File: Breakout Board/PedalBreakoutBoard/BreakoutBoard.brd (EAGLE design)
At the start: 100 x 80 mm, 45 parts, among them U1 ES_DAISY_SEED_REV4

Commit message: DP-16 - Board layout REV-A
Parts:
- removed 1P8T: (no value), SparkFun-Connectors:1X09
- removed GPIOS: (no value), SparkFun-Connectors:1X07
- removed IN_L, IN_R, LED1, LED2, LED3, LED4, OUT_L, OUT_R, SPST1, SPST2, SPST3, SPST4: (no value), SparkFun-Connectors:1X02
- removed POT1, POT2, POT3, POT4, SPDT1, SPDT2: (no value), SparkFun-Connectors:1X03
- added 1P8T_GPIO: (no value), SparkFun-Connectors:1X08
- added 1P8T_PWR: (no value), SparkFun-Connectors:1X01
- added AUDIO, EX_GND, EX_PWR: (no value), SparkFun-Connectors:2X4
- added EX_GPIOS: (no value), SparkFun-Connectors:1X07
- added LED_GND, LED_GPIO, POT_GND, POT_GPIO, POT_PWR, SPDT_GPIO, SPST_GPIO, SPST_PWR: (no value), SparkFun-Connectors:1X04
- added SPDT_PWR: (no value), SparkFun-Connectors:1X02
- moved S1 31.9 mm to (27.9, 47.0)
- moved S2 30.7 mm to (27.9, 44.5)
- moved S3 29.5 mm to (27.9, 41.9)
- moved S4 28.4 mm to (27.9, 39.4)
- moved D11 27.5 mm to (27.9, 36.8)
- moved D12 25.4 mm to (27.9, 34.3)
- moved D21 24.4 mm to (27.9, 31.8)
- moved D22 22.5 mm to (27.9, 29.2)
- moved D1 20.7 mm to (76.2, 62.2)
- moved L4 20.7 mm to (69.8, 19.1)
- moved L3 19.8 mm to (69.8, 21.6)
- moved C3 18.9 mm to (67.3, 63.5), turned to 90 degrees
- moved L2 18.9 mm to (69.8, 24.1)
- moved L1 18.1 mm to (69.8, 26.7)
- moved 8T2 17.3 mm to (73.7, 54.6)
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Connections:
- removed net GPIO10: GPIOS.6, U1.10
- removed net GPIO11: GPIOS.5, U1.11
- removed net GPIO12: GPIOS.4, U1.12
- removed net GPIO13: GPIOS.3, U1.13
- removed net GPIO14: GPIOS.2, U1.14
- removed net GPIO15: GPIOS.1, U1.15
- removed net GPIO9: GPIOS.7, U1.9
- removed net N$6: L2.P$2, LED2.1
- removed net N$7: L3.P$2, LED3.1
- removed net N$8: L4.P$2, LED4.1
- new net GPIO1: EX_GPIOS.7, U1.1
- new net GPIO2: EX_GPIOS.6, U1.2
- new net GPIO3: EX_GPIOS.5, U1.3
- new net GPIO4: EX_GPIOS.4, U1.4
- new net GPIO5: EX_GPIOS.3, U1.5
- new net GPIO6: EX_GPIOS.2, U1.6
- new net GPIO7: EX_GPIOS.1, U1.7
- new net N$1: L1.P$2, LED_GPIO.1
- new net N$3: L2.P$2, LED_GPIO.2
- new net N$4: L3.P$2, LED_GPIO.3
- net +3V3_A: now also 1P8T_PWR.1, EX_PWR.1, EX_PWR.2, EX_PWR.3, EX_PWR.4, EX_PWR.5, EX_PWR.6, EX_PWR.7, EX_PWR.8, POT_PWR.1, POT_PWR.2, POT_PWR.3, POT_PWR.4, SPDT_PWR.1, SPDT_PWR.2, SPST_PWR.1, SPST_PWR.2, SPST_PWR.3, SPST_PWR.4; no longer 1P8T.9, POT1.1, POT2.1, POT3.1, POT4.1, SPDT1.2, SPDT2.2, SPST1.1, SPST2.1, SPST3.1, SPST4.1
- net 1P8T_1: now also 1P8T_GPIO.1; no longer 1P8T.1
- net 1P8T_2: now also 1P8T_GPIO.2; no longer 1P8T.2
- net 1P8T_3: now also 1P8T_GPIO.3; no longer 1P8T.3
- net 1P8T_4: now also 1P8T_GPIO.4; no longer 1P8T.4
- net 1P8T_5: now also 1P8T_GPIO.5; no longer 1P8T.5
- net 1P8T_6: now also 1P8T_GPIO.6; no longer 1P8T.6
- net 1P8T_7: now also 1P8T_GPIO.7; no longer 1P8T.7
- net 1P8T_8: now also 1P8T_GPIO.8; no longer 1P8T.8
- net GND: now also AUDIO.1, AUDIO.3, AUDIO.5, AUDIO.7, EX_GND.1, EX_GND.2, EX_GND.3, EX_GND.4, EX_GND.5, EX_GND.6, EX_GND.7, EX_GND.8, LED_GND.1, LED_GND.2, LED_GND.3, LED_GND.4, POT_GND.1, POT_GND.2, POT_GND.3, POT_GND.4; no longer IN_L.1, IN_R.1, LED1.2, LED2.2, LED3.2, LED4.2, OUT_L.1, OUT_R.1, POT1.3, POT2.3, POT3.3, POT4.3
- net IN_L: now also AUDIO.2; no longer IN_L.2
- net IN_R: now also AUDIO.4; no longer IN_R.2
- net N$5: now also L4.P$2, LED_GPIO.4; no longer L1.P$2, LED1.1
- net OUT_L: now also AUDIO.6; no longer OUT_L.2
- net OUT_R: now also AUDIO.8; no longer OUT_R.2
- net POT1: now also POT_GPIO.1; no longer POT1.2
- net POT2: now also POT_GPIO.2; no longer POT2.2
- net POT3: now also POT_GPIO.3; no longer POT3.2
- net POT4: now also POT_GPIO.4; no longer POT4.2
- net SPDT1_1: now also SPDT_GPIO.4, U1.12; no longer SPDT1.3, U1.5
- net SPDT1_2: now also SPDT_GPIO.3, U1.13; no longer SPDT1.1, U1.6
- net SPDT2_1: now also SPDT_GPIO.2, U1.14; no longer SPDT2.3, U1.7
- net SPDT2_2: now also SPDT_GPIO.1, U1.15; no longer SPDT2.1, U1.8
- net SPST1: now also SPST_GPIO.4, U1.8; no longer SPST1.2, U1.1
- net SPST2: now also SPST_GPIO.3, U1.9; no longer SPST2.2, U1.2
- net SPST3: now also SPST_GPIO.2, U1.10; no longer SPST3.2, U1.3
- net SPST4: now also SPST_GPIO.1, U1.11; no longer SPST4.2, U1.4

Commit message: DP-16 - Board layout REV-B
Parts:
- removed 1P8T_GPIO: (no value), SparkFun-Connectors:1X08
- removed 1P8T_PWR: (no value), SparkFun-Connectors:1X01
- removed 8T1, 8T2, 8T3, 8T4: 10k, SparkFun-Resistors:AXIAL-0.3
- added HEX_GPIO: (no value), SparkFun-Connectors:1X04
- added HEX_PWR: (no value), SparkFun-Connectors:1X01
- EX_GND, EX_PWR: device SparkFun-Connectors:2X4 -> SparkFun-Connectors:1X04
- EX_GPIOS: device SparkFun-Connectors:1X07 -> SparkFun-Connectors:1X04
- moved 8T7 7.62 mm to (73.7, 49.5)
- moved 8T8 7.62 mm to (73.7, 47.0)
- moved 8T5 7.62 mm to (73.7, 54.6)
- moved 8T6 7.62 mm to (73.7, 52.1)
- moved EX_GPIOS 7.62 mm to (35.6, 57.1)
- moved EX_PWR 6.48 mm to (27.9, 57.1), turned to 90 degrees
- moved EX_GND 5.24 mm to (31.8, 57.1), turned to 90 degrees
- moved S3 5.08 mm to (27.9, 47.0)
- moved S4 5.08 mm to (27.9, 44.5)
- moved SPST_GPIO 5.08 mm to (35.6, 44.5)
- moved SPST_PWR 5.08 mm to (20.3, 44.5)
- moved S1 5.08 mm to (27.9, 52.1)
- moved S2 5.08 mm to (27.9, 49.5)
- moved AUDIO 2.54 mm to (34.3, 22.9)
- moved D11 2.54 mm to (27.9, 39.4)
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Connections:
- removed net 1P8T_1: 1P8T_GPIO.1, 8T1.P$2, U1.37
- removed net 1P8T_2: 1P8T_GPIO.2, 8T2.P$2, U1.36
- removed net 1P8T_3: 1P8T_GPIO.3, 8T3.P$2, U1.35
- removed net 1P8T_4: 1P8T_GPIO.4, 8T4.P$2, U1.34
- removed net 1P8T_5: 1P8T_GPIO.5, 8T5.P$2, U1.33
- removed net 1P8T_6: 1P8T_GPIO.6, 8T6.P$2, U1.32
- removed net 1P8T_7: 1P8T_GPIO.7, 8T7.P$2, U1.31
- removed net 1P8T_8: 1P8T_GPIO.8, 8T8.P$2, U1.30
- removed net GPIO5: EX_GPIOS.3, U1.5
- removed net GPIO6: EX_GPIOS.2, U1.6
- removed net GPIO7: EX_GPIOS.1, U1.7
- new net HEX_1: 8T5.P$2, HEX_GPIO.1, U1.36
- new net HEX_2: 8T6.P$2, HEX_GPIO.2, U1.35
- new net HEX_3: 8T7.P$2, HEX_GPIO.3, U1.34
- new net HEX_4: 8T8.P$2, HEX_GPIO.4, U1.33
- net +3V3_A: now also HEX_PWR.1; no longer 1P8T_PWR.1, EX_PWR.5, EX_PWR.6, EX_PWR.7, EX_PWR.8
- net GND: no longer 8T1.P$1, 8T2.P$1, 8T3.P$1, 8T4.P$1, EX_GND.5, EX_GND.6, EX_GND.7, EX_GND.8
- net GPIO1: now also EX_GPIOS.4; no longer EX_GPIOS.7
- net GPIO2: now also EX_GPIOS.3; no longer EX_GPIOS.6
- net GPIO3: now also EX_GPIOS.2; no longer EX_GPIOS.5
- net GPIO4: now also EX_GPIOS.1; no longer EX_GPIOS.4
- net POT1: now also U1.30; no longer U1.29
- net POT2: now also U1.29; no longer U1.28
- net POT3: now also U1.28; no longer U1.27
- net POT4: now also U1.27; no longer U1.26
- net SPDT1_1: now also U1.11; no longer U1.12
- net SPDT1_2: now also U1.12; no longer U1.13
- net SPDT2_1: now also U1.13; no longer U1.14
- net SPDT2_2: now also U1.14; no longer U1.15
- net SPST1: now also U1.6; no longer U1.8
- net SPST2: now also U1.7; no longer U1.9
- net SPST3: now also U1.8; no longer U1.10
- net SPST4: now also U1.9; no longer U1.11
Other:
- board size 100 x 80 mm -> 68.2 x 63.5 mm

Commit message: DP-16 - Initial routing
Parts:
- moved L1 22.2 mm to (50.8, 15.2)
- moved L2 22.2 mm to (50.8, 12.7)
- moved L3 22.2 mm to (50.8, 10.2)
- moved L4 22.2 mm to (50.8, 7.62)
- moved LED_GPIO 22.2 mm to (58.4, 15.2)
- moved D1 21.1 mm to (58.4, 50.8)
- moved C3 20.1 mm to (50.8, 52.1)
- moved D12 20.1 mm to (11.4, 25.4)
- moved D21 20.1 mm to (11.4, 22.9)
- moved D22 20.1 mm to (11.4, 20.3)
- moved EX_GPIOS 20.1 mm to (19.1, 45.7)
- moved EX_PWR 20.1 mm to (11.4, 45.7)
- moved HEX_GPIO 20.1 mm to (49.5, 43.2)
- moved POT_GPIO 20.1 mm to (49.5, 27.9)
- moved PWR 20.1 mm to (57.1, 54.6)
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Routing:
- net GND: track 0.00 -> 176.9 mm, vias 0 -> 1
- net +3V3_A: track 0.00 -> 146.0 mm, vias 0 -> 1
- net +9V_IN: track 0.00 -> 14.8 mm
- net HEX_4: track 0.00 -> 11.6 mm
- net HEX_2: track 0.00 -> 11.6 mm
- net SPST4: track 0.00 -> 11.6 mm
- net SPST2: track 0.00 -> 11.6 mm
- net SPDT2_1: track 0.00 -> 11.6 mm
- net SPDT1_1: track 0.00 -> 11.6 mm
- net HEX_3: track 0.00 -> 11.3 mm
- net HEX_1: track 0.00 -> 11.3 mm
- net SPST3: track 0.00 -> 11.3 mm
- net SPST1: track 0.00 -> 11.3 mm
- net SPDT2_2: track 0.00 -> 11.3 mm
- net SPDT1_2: track 0.00 -> 11.3 mm
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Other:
- board size 68.2 x 63.5 mm -> 64.4 x 58.4 mm

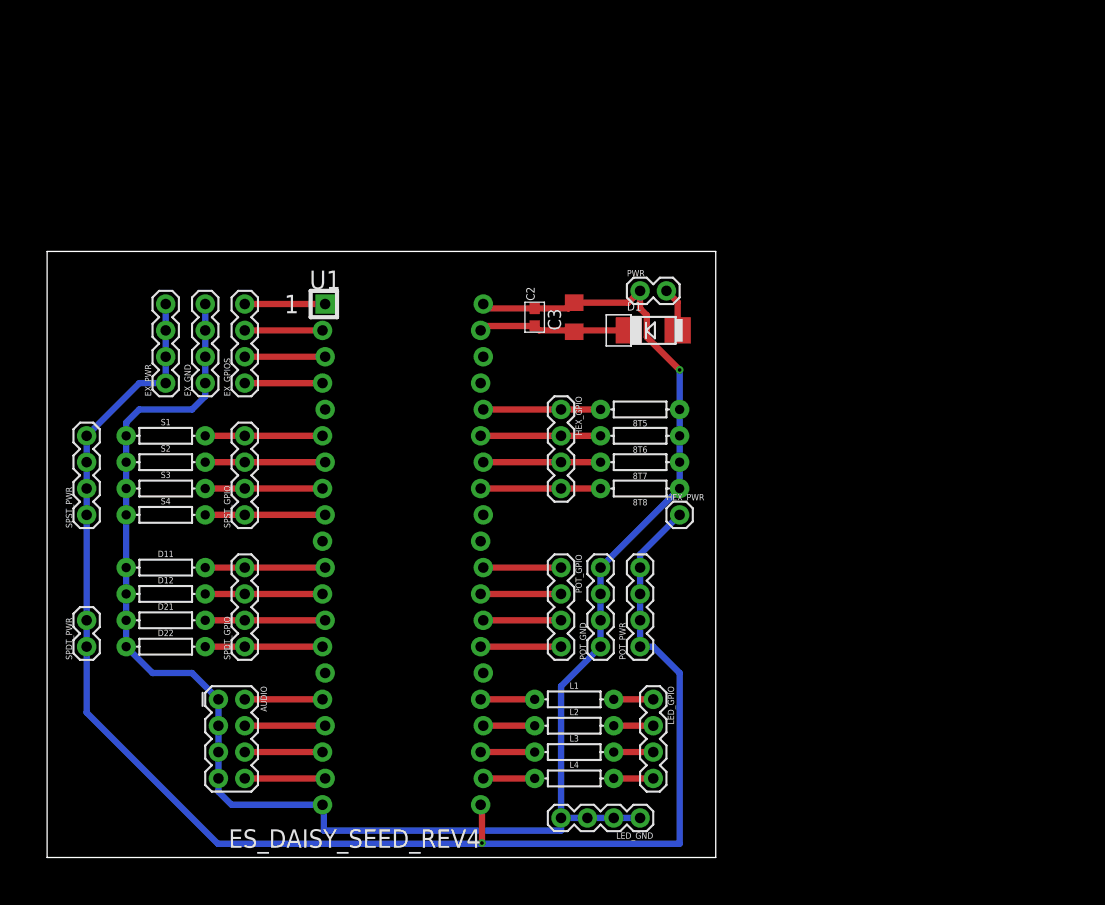
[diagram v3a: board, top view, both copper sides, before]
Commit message: DP-16 - Update board layout
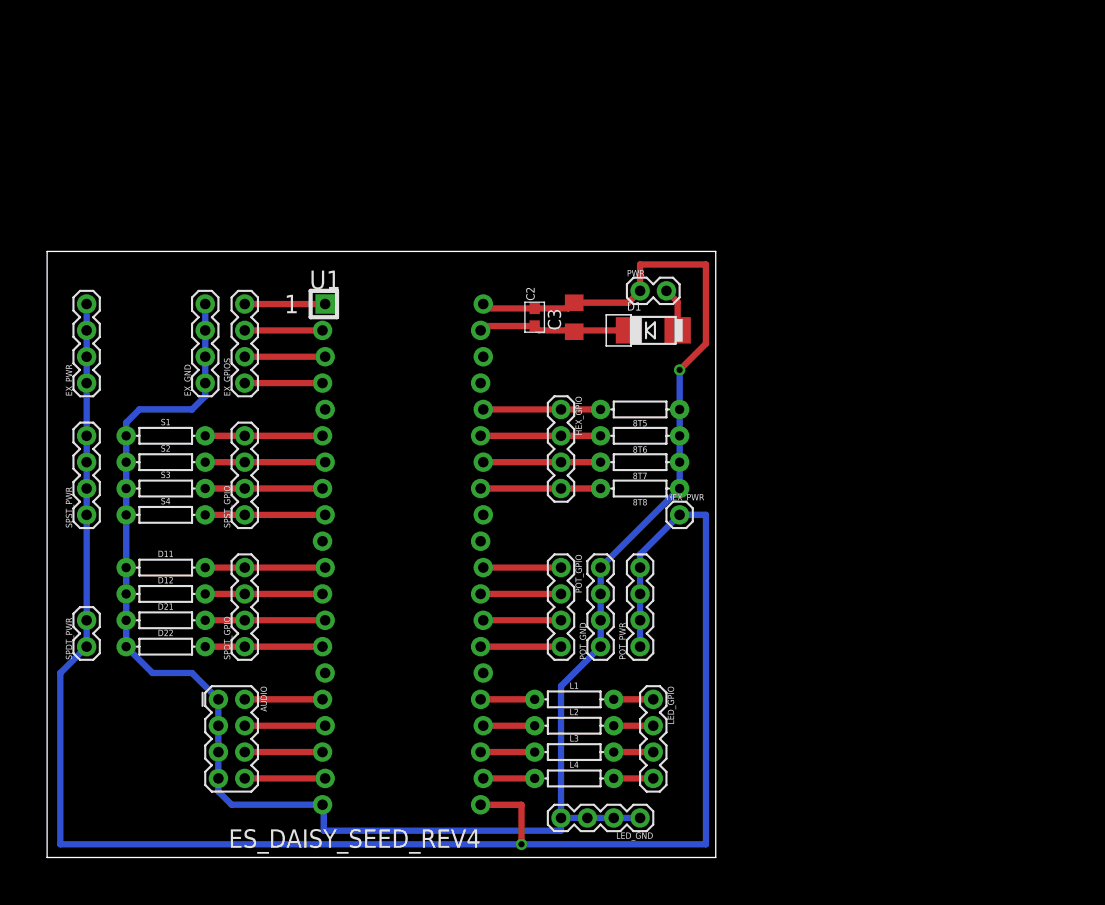
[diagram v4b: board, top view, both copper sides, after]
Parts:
- moved EX_PWR 7.62 mm to (3.81, 45.7)
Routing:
- net +3V3_A: track 146.0 -> 171.7 mm
- net GND: track 176.9 -> 187.8 mm
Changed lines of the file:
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@@
 </class>
 </classes>
-<designrules name="default">
-<description language="de">&lt;b&gt;EAGLE Design Rules&lt;/b&gt;
-&lt;p&gt;
-Die Standard-Design-Rules sind so gewählt, dass sie für
-die meisten Anwendungen passen. Sollte ihre Platine
-besondere Anforderungen haben, treffen Sie die erforderlichen
-Einstellungen hier und speichern die Design Rules unter
-einem neuen Namen ab.</description>
+<designrules name="SparkFun">
 <description language="en">&lt;b&gt;EAGLE Design Rules&lt;/b&gt;
 &lt;p&gt;
@@
 <param name="mtCopper" value="0.035mm 0.035mm 0.035mm 0.035mm 0.035mm 0.035mm 0.035mm 0.035mm 0.035mm 0.035mm 0.035mm 0.035mm 0.035mm 0.035mm 0.035mm 0.035mm"/>
 <param name="mtIsolate" value="1.5mm 0.15mm 0.2mm 0.15mm 0.2mm 0.15mm 0.2mm 0.15mm 0.2mm 0.15mm 0.2mm 0.15mm 0.2mm 0.15mm 0.2mm"/>
-<param name="mdWireWire" value="6mil"/>
-<param name="mdWirePad" value="6mil"/>
-<param name="mdWireVia" value="6mil"/>
-<param name="mdPadPad" value="6mil"/>
-<param name="mdPadVia" value="6mil"/>
-<param name="mdViaVia" value="6mil"/>
-<param name="mdSmdPad" value="6mil"/>
-<param name="mdSmdVia" value="6mil"/>
-<param name="mdSmdSmd" value="6mil"/>
-<param name="mdViaViaSameLayer" value="6mil"/>
+<param name="mdWireWire" value="8mil"/>
+<param name="mdWirePad" value="8mil"/>
+<param name="mdWireVia" value="8mil"/>
+<param name="mdPadPad" value="8mil"/>
+<param name="mdPadVia" value="8mil"/>
+<param name="mdViaVia" value="8mil"/>
+<param name="mdSmdPad" value="8mil"/>
+<param name="mdSmdVia" value="8mil"/>
+<param name="mdSmdSmd" value="8mil"/>
+<param name="mdViaViaSameLayer" value="8mil"/>
 <param name="mnLayersViaInSmd" value="2"/>
-<param name="mdCopperDimension" value="40mil"/>
-<param name="mdDrill" value="6mil"/>
+<param name="mdCopperDimension" value="8mil"/>
+<param name="mdDrill" value="8mil"/>
 <param name="mdSmdStop" value="0mil"/>
-<param name="msWidth" value="6mil"/>
-<param name="msDrill" value="0.35mm"/>
+<param name="msWidth" value="8mil"/>
+<param name="msDrill" value="20mil"/>
 <param name="msMicroVia" value="9.99mm"/>
 <param name="msBlindViaRatio" value="0.5"/>
@@
 <param name="rvMicroViaOuter" value="0.25"/>
 <param name="rvMicroViaInner" value="0.25"/>
-<param name="rlMinPadTop" value="10mil"/>
+<param name="rlMinPadTop" value="12mil"/>
 <param name="rlMaxPadTop" value="20mil"/>
 <param name="rlMinPadInner" value="10mil"/>
 <param name="rlMaxPadInner" value="20mil"/>
-<param name="rlMinPadBottom" value="10mil"/>
+<param name="rlMinPadBottom" value="12mil"/>
 <param name="rlMaxPadBottom" value="20mil"/>
-<param name="rlMinViaOuter" value="8mil"/>
+<param name="rlMinViaOuter" value="10mil"/>
 <param name="rlMaxViaOuter" value="20mil"/>
-<param name="rlMinViaInner" value="8mil"/>
+<param name="rlMinViaInner" value="10mil"/>
 <param name="rlMaxViaInner" value="20mil"/>
 <param name="rlMinMicroViaOuter" value="4mil"/>
@@
 <param name="mlMinCreamFrame" value="0mil"/>
 <param name="mlMaxCreamFrame" value="0mil"/>
-<param name="mlViaStopLimit" value="0mil"/>
+<param name="mlViaStopLimit" value="20mil"/>
 <param name="srRoundness" value="0"/>
 <param name="srMinRoundness" value="0mil"/>
@@
 <attribute name="VALUE" x="21.082" y="44.45" size="0.6096" layer="27" font="vector" ratio="20" rot="R90"/>
 </element>
-<element name="EX_PWR" library="SparkFun-Connectors" library_urn="urn:adsk.eagle:library:513" package="1X04" package3d_urn="urn:adsk.eagle:package:38085/1" value="" x="11.43" y="45.72" smashed="yes" rot="R90">
-<attribute name="NAME" x="10.033" y="44.45" size="0.6096" layer="25" font="vector" ratio="20" rot="R90"/>
-<attribute name="PROD_ID" value="CONN-09696" x="11.43" y="45.72" size="1.778" layer="27" rot="R90" display="off"/>
-<attribute name="VALUE" x="13.462" y="44.45" size="0.6096" layer="27" font="vector" ratio="20" rot="R90"/>
+<element name="EX_PWR" library="SparkFun-Connectors" library_urn="urn:adsk.eagle:library:513" package="1X04" package3d_urn="urn:adsk.eagle:package:38085/1" value="" x="3.81" y="45.72" smashed="yes" rot="R90">
+<attribute name="NAME" x="2.413" y="44.45" size="0.6096" layer="25" font="vector" ratio="20" rot="R90"/>
+<attribute name="PROD_ID" value="CONN-09696" x="3.81" y="45.72" size="1.778" layer="27" rot="R90" display="off"/>
+<attribute name="VALUE" x="5.842" y="44.45" size="0.6096" layer="27" font="vector" ratio="20" rot="R90"/>
 </element>
 <element name="EX_GND" library="SparkFun-Connectors" library_urn="urn:adsk.eagle:library:513" package="1X04" package3d_urn="urn:adsk.eagle:package:38085/1" value="" x="15.24" y="45.72" smashed="yes" rot="R90">
@@
 <wire x1="60.96" y1="40.64" x2="60.96" y2="43.18" width="0.6096" layer="16"/>
 <wire x1="60.96" y1="43.18" x2="60.96" y2="46.99" width="0.6096" layer="16"/>
-<via x="60.96" y="46.99" extent="1-16" drill="0.35"/>
-<wire x1="60.96" y1="46.99" x2="57.7977" y2="50.1523" width="0.6096" layer="1"/>
-<wire x1="57.7977" y1="50.1523" x2="57.7977" y2="52.25938125" width="0.6096" layer="1"/>
-<wire x1="57.15" y1="52.90708125" x2="57.15" y2="54.61" width="0.6096" layer="1"/>
-<wire x1="57.7977" y1="52.25938125" x2="57.15" y2="52.90708125" width="0.6096" layer="1"/>
+<via x="60.96" y="46.99" extent="1-16" drill="0.6"/>
 <wire x1="57.15" y1="54.61" x2="56.01" y2="53.47" width="0.6096" layer="1"/>
 <wire x1="56.01" y1="53.47" x2="50.8" y2="53.47" width="0.6096" layer="1"/>
@@
 <wire x1="46.99" y1="52.92" x2="42.457" y2="52.92" width="0.6096" layer="1"/>
 <wire x1="42.457" y1="52.92" x2="42.037" y2="53.34" width="0.6096" layer="1"/>
+<wire x1="60.96" y1="46.99" x2="63.5" y2="49.53" width="0.6096" layer="1"/>
+<wire x1="63.5" y1="49.53" x2="63.5" y2="57.15" width="0.6096" layer="1"/>
+<wire x1="63.5" y1="57.15" x2="57.15" y2="57.15" width="0.6096" layer="1"/>
+<wire x1="57.15" y1="57.15" x2="57.15" y2="54.61" width="0.6096" layer="1"/>
 </signal>
 <signal name="SPST1">
@@
 <contactref element="EX_PWR" pad="3"/>
 <contactref element="EX_PWR" pad="4"/>
-<wire x1="41.91" y1="4.953" x2="41.783" y2="5.08" width="0.6096" layer="1"/>
-<wire x1="41.783" y1="5.08" x2="41.8465" y2="5.0165" width="0.6096" layer="1"/>
-<wire x1="41.91" y1="4.953" x2="41.91" y2="1.3942" width="0.6096" layer="1"/>
-<wire x1="41.91" y1="1.3942" x2="41.91" y2="1.3208" width="0.6096" layer="1"/>
-<via x="41.91" y="1.3942" extent="1-16" drill="0.35"/>
-<wire x1="41.91" y1="1.3942" x2="41.9721" y2="1.3321" width="0.6096" layer="16"/>
-<wire x1="41.9721" y1="1.3321" x2="41.9834" y2="1.3208" width="0.6096" layer="16"/>
-<wire x1="41.9834" y1="1.3208" x2="60.96" y2="1.3208" width="0.6096" layer="16"/>
-<wire x1="60.96" y1="1.3208" x2="60.96" y2="17.78" width="0.6096" layer="16"/>
-<wire x1="60.96" y1="17.78" x2="58.42" y2="20.32" width="0.6096" layer="16"/>
-<wire x1="58.42" y1="20.32" x2="57.15" y2="20.32" width="0.6096" layer="16"/>
 <wire x1="57.15" y1="20.32" x2="57.15" y2="22.86" width="0.6096" layer="16"/>
 <wire x1="57.15" y1="22.86" x2="57.15" y2="25.4" width="0.6096" layer="16"/>
 <wire x1="57.15" y1="25.4" x2="57.15" y2="27.94" width="0.6096" layer="16"/>
-<wire x1="57.15" y1="27.94" x2="57.15" y2="29.21" width="0.6096" layer="16"/>
-<wire x1="57.15" y1="29.21" x2="60.96" y2="33.02" width="0.6096" layer="16"/>
-<wire x1="3.81" y1="20.32" x2="3.81" y2="13.97" width="0.6096" layer="16"/>
-<wire x1="3.81" y1="13.97" x2="16.4592" y2="1.3208" width="0.6096" layer="16"/>
-<wire x1="41.9608" y1="1.3208" x2="41.9721" y2="1.3321" width="0.6096" layer="16"/>
-<wire x1="16.4592" y1="1.3208" x2="41.9608" y2="1.3208" width="0.6096" layer="16"/>
+<wire x1="57.15" y1="29.21" x2="57.15" y2="27.94" width="0.6096" layer="16"/>
 <wire x1="3.81" y1="20.32" x2="3.81" y2="22.86" width="0.6096" layer="16"/>
 <wire x1="3.81" y1="22.86" x2="3.81" y2="33.02" width="0.6096" layer="16"/>
@@
 <wire x1="3.81" y1="35.56" x2="3.81" y2="38.1" width="0.6096" layer="16"/>
 <wire x1="3.81" y1="38.1" x2="3.81" y2="40.64" width="0.6096" layer="16"/>
-<wire x1="3.81" y1="40.64" x2="8.89" y2="45.72" width="0.6096" layer="16"/>
-<wire x1="8.89" y1="45.72" x2="11.43" y2="45.72" width="0.6096" layer="16"/>
-<wire x1="11.43" y1="45.72" x2="11.43" y2="48.26" width="0.6096" layer="16"/>
-<wire x1="11.43" y1="48.26" x2="11.43" y2="50.8" width="0.6096" layer="16"/>
-<wire x1="11.43" y1="50.8" x2="11.43" y2="53.34" width="0.6096" layer="16"/>
+<wire x1="3.81" y1="20.32" x2="1.27" y2="17.78" width="0.6096" layer="16"/>
+<wire x1="1.27" y1="17.78" x2="1.27" y2="1.27" width="0.6096" layer="16"/>
+<wire x1="63.5" y1="1.27" x2="63.5" y2="33.02" width="0.6096" layer="16"/>
+<wire x1="60.96" y1="33.02" x2="63.5" y2="33.02" width="0.6096" layer="16"/>
+<wire x1="60.96" y1="33.02" x2="57.15" y2="29.21" width="0.6096" layer="16"/>
+<wire x1="41.783" y1="5.08" x2="45.72" y2="5.08" width="0.6096" layer="1"/>
+<wire x1="45.72" y1="5.08" x2="45.72" y2="1.27" width="0.6096" layer="1"/>
+<via x="45.72" y="1.27" extent="1-16" drill="0.6"/>
+<wire x1="45.72" y1="1.27" x2="63.5" y2="1.27" width="0.6096" layer="16"/>
+<wire x1="1.27" y1="1.27" x2="45.72" y2="1.27" width="0.6096" layer="16"/>
+<wire x1="3.81" y1="40.64" x2="3.81" y2="45.72" width="0.6096" layer="16"/>
+<wire x1="3.81" y1="45.72" x2="3.81" y2="48.26" width="0.6096" layer="16"/>
+<wire x1="3.81" y1="48.26" x2="3.81" y2="50.8" width="0.6096" layer="16"/>
+<wire x1="3.81" y1="50.8" x2="3.81" y2="53.34" width="0.6096" layer="16"/>
 </signal>
 <signal name="SPDT1_1">

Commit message: DP-16 - Working on silkscreen and mounting holes
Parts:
- renumbered 8T5 to H1, 8T6 to H2, 8T7 to H3, 8T8 to H4, U1 to SEED
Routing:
- added copper zone on layer 1, net GND
- added copper zone on layer 16, net GND
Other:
- board size 64.4 x 58.4 mm -> 69.5 x 63.5 mm
- board text added: "Pedal Breakout Board REV: A"
- board text added: "Saved By Grace Software"
